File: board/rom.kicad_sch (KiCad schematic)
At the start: 4 parts, among them U2 ROM LO, U3 ROM HI

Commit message: fill out most functionality - passes ERC
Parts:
- renumbered C1 to C6, C2 to C7
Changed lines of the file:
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@@
 	)
 	(global_label "D15"
-		(shape tri_state)
+		(shape output)
 		(at 99.06 139.7 0)
 		(fields_autoplaced yes)
@@
 	)
 	(global_label "D8"
-		(shape tri_state)
+		(shape output)
 		(at 99.06 121.92 0)
 		(fields_autoplaced yes)
@@
 	)
 	(global_label "D13"
-		(shape tri_state)
+		(shape output)
 		(at 99.06 134.62 0)
 		(fields_autoplaced yes)
@@
 	)
 	(global_label "D0"
-		(shape tri_state)
+		(shape output)
 		(at 99.06 38.1 0)
 		(fields_autoplaced yes)
@@
 	)
 	(global_label "D2"
-		(shape tri_state)
+		(shape output)
 		(at 99.06 43.18 0)
 		(fields_autoplaced yes)
@@
 	)
 	(global_label "D6"
-		(shape tri_state)
+		(shape output)
 		(at 99.06 53.34 0)
 		(fields_autoplaced yes)
@@
 	)
 	(global_label "D12"
-		(shape tri_state)
+		(shape output)
 		(at 99.06 132.08 0)
 		(fields_autoplaced yes)
@@
 	)
 	(global_label "D9"
-		(shape tri_state)
+		(shape output)
 		(at 99.06 124.46 0)
 		(fields_autoplaced yes)
@@
 	)
 	(global_label "D11"
-		(shape tri_state)
+		(shape output)
 		(at 99.06 129.54 0)
 		(fields_autoplaced yes)
@@
 	)
 	(global_label "D4"
-		(shape tri_state)
+		(shape output)
 		(at 99.06 48.26 0)
 		(fields_autoplaced yes)
@@
 	)
 	(global_label "D3"
-		(shape tri_state)
+		(shape output)
 		(at 99.06 45.72 0)
 		(fields_autoplaced yes)
@@
 	)
 	(global_label "D5"
-		(shape tri_state)
+		(shape output)
 		(at 99.06 50.8 0)
 		(fields_autoplaced yes)
@@
 	)
 	(global_label "D7"
-		(shape tri_state)
+		(shape output)
 		(at 99.06 55.88 0)
 		(fields_autoplaced yes)
@@
 	)
 	(global_label "D1"
-		(shape tri_state)
+		(shape output)
 		(at 99.06 40.64 0)
 		(fields_autoplaced yes)
@@
 	)
 	(global_label "D10"
-		(shape tri_state)
+		(shape output)
 		(at 99.06 127 0)
 		(fields_autoplaced yes)
@@
 	)
 	(global_label "D14"
-		(shape tri_state)
+		(shape output)
 		(at 99.06 137.16 0)
 		(fields_autoplaced yes)
@@
 		(dnp no)
 		(fields_autoplaced yes)
-		(property "Reference" "#PWR010"
+		(property "Reference" "#PWR028"
 			(at 82.55 179.07 0)
 			(effects
@@
 			(project "board"
 				(path "/afefa398-9f39-4b22-97f8-dae9b102df0d/3a4dea8d-1857-4b43-8092-baf1d8c2c547"
-					(reference "#PWR010")
+					(reference "#PWR028")
 					(unit 1)
 				)
@@
 		(dnp no)
 		(fields_autoplaced yes)
-		(property "Reference" "#PWR03"
+		(property "Reference" "#PWR025"
 			(at 82.55 36.83 0)
 			(effects
@@
 			(project ""
 				(path "/afefa398-9f39-4b22-97f8-dae9b102df0d/3a4dea8d-1857-4b43-8092-baf1d8c2c547"
-					(reference "#PWR03")
+					(reference "#PWR025")
 					(unit 1)
 				)
@@
 		(dnp no)
 		(fields_autoplaced yes)
-		(property "Reference" "#PWR04"
+		(property "Reference" "#PWR022"
 			(at 33.02 97.79 0)
 			(effects
@@
 			(project "board"
 				(path "/afefa398-9f39-4b22-97f8-dae9b102df0d/3a4dea8d-1857-4b43-8092-baf1d8c2c547"
-					(reference "#PWR04")
+					(reference "#PWR022")
 					(unit 1)
 				)
@@
 		(dnp no)
 		(fields_autoplaced yes)
-		(property "Reference" "C1"
+		(property "Reference" "C6"
 			(at 36.83 86.3599 0)
 			(effects
@@
 			(project ""
 				(path "/afefa398-9f39-4b22-97f8-dae9b102df0d/3a4dea8d-1857-4b43-8092-baf1d8c2c547"
-					(reference "C1")
+					(reference "C6")
 					(unit 1)
 				)
@@
 		(dnp no)
 		(fields_autoplaced yes)
-		(property "Reference" "#PWR07"
+		(property "Reference" "#PWR023"
 			(at 34.29 172.72 0)
 			(effects
@@
 			(project "board"
 				(path "/afefa398-9f39-4b22-97f8-dae9b102df0d/3a4dea8d-1857-4b43-8092-baf1d8c2c547"
-					(reference "#PWR07")
+					(reference "#PWR023")
 					(unit 1)
 				)
@@
 		(dnp no)
 		(fields_autoplaced yes)
-		(property "Reference" "C2"
+		(property "Reference" "C7"
 			(at 38.1 171.4499 0)
 			(effects
@@
 			(project "board"
 				(path "/afefa398-9f39-4b22-97f8-dae9b102df0d/3a4dea8d-1857-4b43-8092-baf1d8c2c547"
-					(reference "C2")
+					(reference "C7")
 					(unit 1)
 				)
@@
 		(dnp no)
 		(fields_autoplaced yes)
-		(property "Reference" "#PWR05"
+		(property "Reference" "#PWR026"
 			(at 82.55 95.25 0)
 			(effects
@@
 			(project ""
 				(path "/afefa398-9f39-4b22-97f8-dae9b102df0d/3a4dea8d-1857-4b43-8092-baf1d8c2c547"
-					(reference "#PWR05")
+					(reference "#PWR026")
 					(unit 1)
 				)
@@
 		(dnp no)
 		(fields_autoplaced yes)
-		(property "Reference" "#PWR09"
+		(property "Reference" "#PWR027"
 			(at 82.55 120.65 0)
 			(effects
@@
 			(project "board"
 				(path "/afefa398-9f39-4b22-97f8-dae9b102df0d/3a4dea8d-1857-4b43-8092-baf1d8c2c547"
-					(reference "#PWR09")
+					(reference "#PWR027")
 					(unit 1)
 				)
@@
 		(dnp no)
 		(fields_autoplaced yes)
-		(property "Reference" "#PWR06"
+		(property "Reference" "#PWR021"
 			(at 33.02 87.63 0)
 			(effects
@@
 			(project "board"
 				(path "/afefa398-9f39-4b22-97f8-dae9b102df0d/3a4dea8d-1857-4b43-8092-baf1d8c2c547"
-					(reference "#PWR06")
+					(reference "#PWR021")
 					(unit 1)
 				)
@@
 		(dnp no)
 		(fields_autoplaced yes)
-		(property "Reference" "#PWR08"
+		(property "Reference" "#PWR024"
 			(at 34.29 182.88 0)
 			(effects
@@
 			(project "board"
 				(path "/afefa398-9f39-4b22-97f8-dae9b102df0d/3a4dea8d-1857-4b43-8092-baf1d8c2c547"
-					(reference "#PWR08")
+					(reference "#PWR024")
 					(unit 1)
 				)

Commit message: design draft complete, added footprints
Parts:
- C6, C7: footprint (none) -> Capacitor_THT:C_Disc_D5.0mm_W2.5mm_P5.00mm
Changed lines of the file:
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@@
 			)
 		)
-		(property "Footprint" ""
+		(property "Footprint" "Capacitor_THT:C_Disc_D5.0mm_W2.5mm_P5.00mm"
 			(at 33.9852 91.44 0)
 			(effects
@@
 			)
 		)
-		(property "Footprint" ""
+		(property "Footprint" "Capacitor_THT:C_Disc_D5.0mm_W2.5mm_P5.00mm"
 			(at 35.2552 176.53 0)
 			(effects

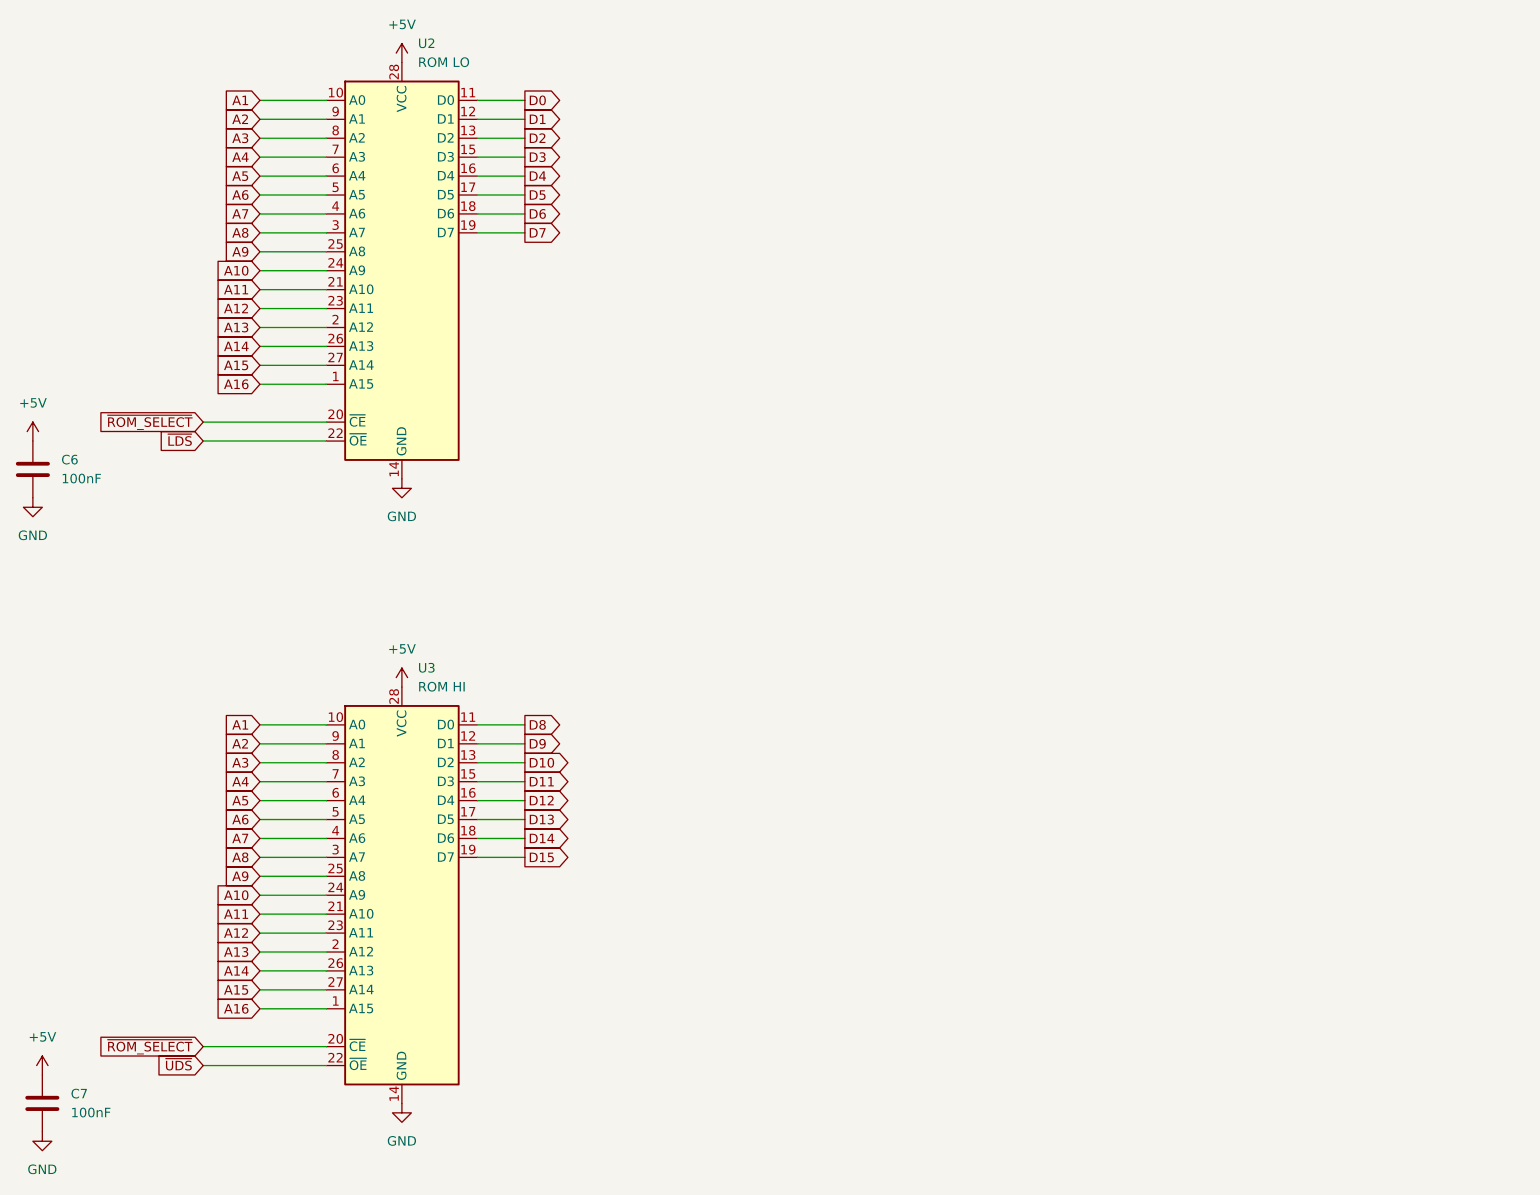
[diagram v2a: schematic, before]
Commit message: start of PCB and MMU
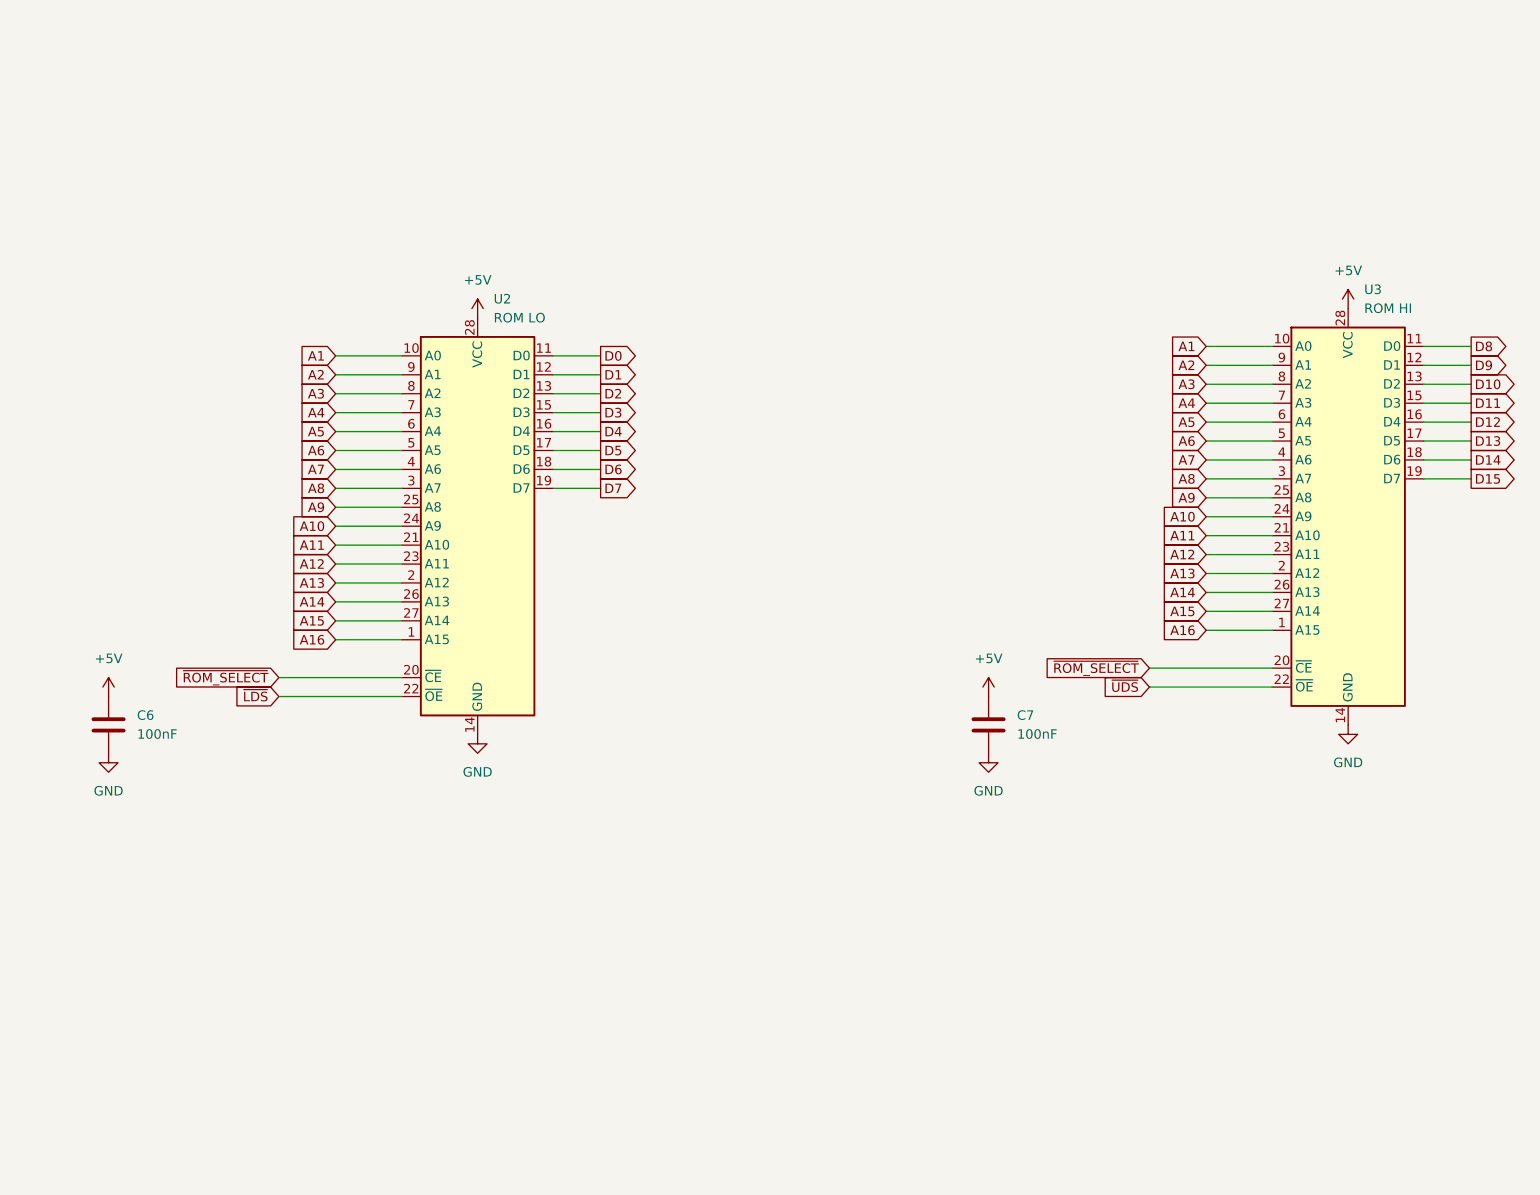
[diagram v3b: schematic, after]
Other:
- moved on the sheet: C6, C7, U2, U3
